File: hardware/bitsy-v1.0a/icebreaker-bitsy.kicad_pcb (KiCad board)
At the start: 4 copper layers, 35.6 x 17.8 mm, 94 parts, among them J1 3V3, J10 4, J11 1, J12 5, J13 7, J14 6, J15 16, J16 15, J17 18, J18 17, J19 19, J2 3V3, J20 20, J21 21, J22 22, J23 23, J24 8, J25 9, J26 13, J27 14, J28 12, J29 11, J3 VIN, J30 10, J31 CDONE, J32 CRESET, J33 USB_C, J34 PROG, J4 GND, J5 GND, J6 GND, J7 2, J8 3, J9 0, P1 UP, P2 UP, P3 UP, P4 UP, SW1 TACT, U1 USBLC6-2, U2 TLV75512PDRV, U3 TLV75533PDRV, U4 LY68L6400, U5 W25Q, U6 ICE40UP5K-SG48, X1 12MHz

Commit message: Final bitsy-v1.0a
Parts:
- added REF**: Symbol_CC-SA_SilkScreen_1mm, pkl_logos:Symbol_CC-SA_SilkScreen_1mm, B.Cu at (42.5, 50.6)
- added REF**: Symbol_CC-BY_SilkScreen_1mm, pkl_logos:Symbol_CC-BY_SilkScreen_1mm, B.Cu at (42.5, 49.4)
- added REF**: Symbol_CC_SilkScreen_2mm, pkl_logos:Symbol_CC_SilkScreen_2mm, B.Cu at (43.0, 47.7)
- J33: footprint Connector_USB:USB_C_Receptacle_HRO_TYPE-C-31-M-12 -> pkl_connectors:USB_C_Receptacle_HRO_TYPE-C-31-M-12
- JP1, JP5: footprint pkl_jumpers:J_NC_0603_20x2 -> pkl_jumpers:J_NC_0603_40
- moved JP1 0.64 mm to (36.5, 45.0), turned to 90 degrees
- moved JP2 0.50 mm to (44.0, 46.0)
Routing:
- net VBUS: track 16.1 -> 21.9 mm, vias 3 -> 2
- net VIN: track 23.7 -> 24.8 mm
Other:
- board text added: "BY"
- board text added: "SA"
- board text added: "by Jordi @0xdec"
- board text added: "v1.0a"
- board text removed: "CC BY-SA"
- board text removed: "USB"
- board text removed: "V1.0a"

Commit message: WIP pin shuffling
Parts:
- removed the J11 at (36.4, 55.1)
- added J10: 3, pkl_pin_headers:Pin_Header_Straight_Round_1x01_Castellated, F.Cu at (41.4, 55.1)
- J7: renamed from J8; value 3 -> 2
- J8: renamed from J7; value 2 -> 0
- J9: value 0 -> 1
- moved R1 5.91 mm to (37.1, 52.9), turned to 270 degrees
- moved J8 5.08 mm to (33.8, 55.1)
- moved J7 2.54 mm to (38.9, 55.1)
- moved J9 2.54 mm to (36.4, 55.1)
- moved C7 0.78 mm to (53.3, 52.5), turned to 90 degrees
- renumbered J10 to J11, J14 to J13, J13 to J14, J16 to J15, J15 to J16, J19 to J18, J18 to J19, J30 to J26, J29 to J27, J26 to J29, J27 to J30
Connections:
- net /IOB_3B_G6 renamed /IOB_3b_G6
- net /IOB_6A renamed /IOB_6a
- net /IOT_38B renamed /IOT_38b
- net /IOT_42B renamed /IOT_42b
- net /IOT_43A renamed /IOT_43a
- net /IOT_44B renamed /IOT_44b
- net /iCE_SS_B renamed /iCE_SS
- J11 pad 1: /IOB_4A -> /IOB_5b
- J13 pad 1: /IOB_9B -> /IOB_8a
- J14 pad 1: /IOB_8A -> /IOB_9b
- J15 pad 1: /IOT_37A -> /IOT_36b
- J16 pad 1: /IOT_36B -> /IOT_37a
- J18 pad 1: /IOT_41A -> /IOT_39a
- J19 pad 1: /IOT_39A -> /IOT_41a
- J23 pad 1: /IOT_48B -> /IOT_50b
- J24 pad 1: /IOB_13B -> /IOB_13b
- J25 pad 1: /IOB_16A -> /IOB_18a
- J26 pad 1: /IOB_31B -> /IOB_20a
- J27 pad 1: /IOB_29B -> /IOB_22a
- J28 pad 1: /IOB_25B_G3 -> /IOB_23b
- J30 pad 1: /IOB_23B -> /IOB_25b_G3
- J7 pad 1: /IOB_2A -> /IOB_0a
- J8 pad 1: /IOB_0A -> /IOB_2a
- U6 pad 10: /~UBTN -> /IOB_18a
- U6 pad 11: /~LEDR -> /IOB_20a
- U6 pad 12: /FLASH_~WP~-IO2 -> /IOB_22a
- U6 pad 13: /FLASH_~HLD~-IO3 -> /~LEDR
- U6 pad 18: /IOB_31B -> /FLASH_~WP~-IO2
- U6 pad 19: /IOB_29B -> /FLASH_~HLD~-IO3
- U6 pad 20: /IOB_25B_G3 -> /IOB_25b_G3
- U6 pad 21: /IOB_23B -> /IOB_23b
- U6 pad 23: /IOT_37A -> /IOT_37a
- U6 pad 25: /IOT_36B -> /IOT_36b
- U6 pad 26: /IOT_39A -> /IOT_39a
- U6 pad 28: /IOT_41A -> /IOT_41a
- U6 pad 3: /IOB_9B -> /IOB_9b
- U6 pad 36: /IOT_48B -> /~UBTN
- U6 pad 37: /~LEDG -> /USB_DET
- U6 pad 38: /USB_DET -> /IOT_50b
- U6 pad 4: /IOB_8A -> /IOB_8a
- U6 pad 45: /IOB_5B -> /IOB_5b
- U6 pad 46: /IOB_0A -> /IOB_0a
- U6 pad 47: /IOB_2A -> /IOB_2a
- U6 pad 48: /IOB_4A -> /IOB_4a
- U6 pad 6: /IOB_13B -> /~LEDG
- U6 pad 9: /IOB_16A -> /IOB_13b
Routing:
- net /~LEDR: track 67.9 -> 0.00 mm, vias 5 -> 0
- net /RAM_SS: track 28.2 -> 0.00 mm, vias 3 -> 0
- net /IOB_25B_G3: track 17.1 -> 0.00 mm, vias 1 -> 0
- net /IOB_23b: track 0.00 -> 16.9 mm, vias 0 -> 1
- net /IOB_29B: track 14.5 -> 0.00 mm, vias 1 -> 0
- net /IOB_25b_G3: track 0.00 -> 14.2 mm, vias 0 -> 1
- net /IOB_3b_G6: track 15.1 -> 0.99 mm
- net /IOB_31B: track 13.6 -> 0.00 mm, vias 1 -> 0
- net /IOB_23B: track 13.5 -> 0.00 mm, vias 1 -> 0
- net /~UBTN: track 20.1 -> 7.31 mm, vias 2 -> 0
- net /IOB_5B: track 12.4 -> 0.00 mm, vias 1 -> 0
- net /IOB_22a: track 0.00 -> 12.4 mm
- net /IOT_48B: track 12.1 -> 0.00 mm, vias 1 -> 0
- net /IOB_0A: track 10.6 -> 0.00 mm, vias 1 -> 0
- net /IOB_20a: track 0.00 -> 10.3 mm
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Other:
- board text added: "+"
- board text added: "+IOB_22a 12 11"
- board text added: "+IOB_2a 47 00"
- board text added: "+IOB_4a 48 03"
- board text added: "+IOB_8a 04 06"
- board text added: "-"
- board text added: "-IOB_23b 21 12"
- board text added: "-IOB_5b 45 04"
- board text added: "-IOB_9b 03 07"
- board text added: "/"
- board text added: "13 13 IOB_24a+ ~LEDR"
- board text added: "14 20 IOB_25b- G3"
- board text added: "15 25 IOT_36b-"
- board text added: "16 23 IOT_37a+"
- board text added: "17 28 IOT_41a"
- board text added: "18 27 IOT_38b-"
- board text added: "19 26 IOT_39a+"
- board text added: "20 31 IOT_42b-"
- board text added: "21 32 IOT_43a+"
- board text added: "22 34 IOT_44b"
- board text added: "23 38 IOT_50b"
- board text added: "25"
- board text added: "26"
- board text added: "27"
- board text added: "28"
- board text added: "31"
- board text added: "32"
- board text added: "34"
- board text added: "36"
- board text added: "44"
- board text added: "45"
- board text added: "46"
- board text added: "47"
- board text added: "48"
- board text added: "G6 -IOB_3b 44 01"
- board text added: "IOB_0a 46 02"
- board text added: "IOB_16a 09 08"
- board text added: "IOB_18a 10 09"
- board text added: "IOB_20a 11 10"
- board text added: "IOB_6a 02 05"
- board text added: "R"
- board text removed: "0"
- board text removed: "1"
- board text removed: "10"
- board text removed: "11"
- board text removed: "13"
- board text removed: "13 IOB_20A-~LEDR"
- board text removed: "14"
- board text removed: "14 IOB_23B"
- board text removed: "15"
- board text removed: "15 IOT_37A"
- board text removed: "16"
- board text removed: "16 IOT_36B"
- board text removed: "17"
- board text removed: "17 IOT_39A"
- board text removed: "18 IOT_38B"
- board text removed: "19 IOT_41A"
- board text removed: "20 IOT_42B"
- board text removed: "21 IOT_43A"
- board text removed: "22"
- board text removed: "22 IOT_44B"
- board text removed: "23 IOT_48B"
- board text removed: "5"
- board text removed: "7"
- board text removed: "8"
- board text removed: "IOB_0A 02"
- board text removed: "IOB_13B 08"
- board text removed: "IOB_16A 09"
- board text removed: "IOB_25B_G3 12"
- board text removed: "IOB_29B 11"
- board text removed: "IOB_2A 03"
- board text removed: "IOB_31B 10"
- board text removed: "IOB_3B_G6 00"
- board text removed: "IOB_4A 04"
- board text removed: "IOB_5B 01"
- board text removed: "IOB_6A 05"
- board text removed: "IOB_8A 07"
- board text removed: "IOB_9B 06"

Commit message: Final bitsy-v1.0a (for real this time)
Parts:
- removed C20: 10u, pkl_dipol:C_0603
- removed J34: PROG, pkl_pin_headers:PinHeader_2x05_P2.54mm_Vertical_SMD
- removed JP7, JP8: Jumper, pkl_jumpers:J_NC_0603_30
- removed R15: 2k2, pkl_dipol:R_0402
- added J0: 0, pkl_pin_headers:Pin_Header_Straight_Round_1x01_Castellated, F.Cu at (103.8, 107.6)
- added REF**: 1b2_Logo_SilkS_2mm, pkl_logos:1b2_Logo_SilkS_2mm, F.Cu at (122.4, 104.9)
- C1: value 4u7 -> 1u; footprint pkl_dipol:C_0603 -> pkl_dipol:C_0402
- C19: value 100n -> 10u; footprint pkl_dipol:C_0402 -> pkl_dipol:C_0603
- C3: value 1u -> 4u7; footprint pkl_dipol:C_0402 -> pkl_dipol:C_0603
- J1: value 3V3 -> 1
- J10: value 3 -> 10
- J11: value 4 -> 11
- J12: value 5 -> 12
- J13: value 6 -> 13
- J14: value 7 -> 14
- J17: value 18 -> 17
- J18: value 19 -> 18
- J19: value 17 -> 19
- J2: value 3V3 -> 2
- J24: value 8 -> GND
- J25: value 9 -> GND
- J26: value 10 -> GND
- J27: value 11 -> 3V3
- J28: value 12 -> 3V3
- J29: value 13 -> VIN
- J3: value VIN -> 3
- J30: value 14 -> CDONE
- J31: value CDONE -> CRESET
- J32: value CRESET -> PROG; footprint pkl_pin_headers:Pin_Header_Straight_Round_1x01_Castellated -> pkl_pin_headers:PinHeader_2x05_P2.54mm_Vertical_SMD; moved to B.Cu
- J4: value GND -> 4
- J5: value GND -> 5
- J6: value GND -> 6
- J7: value 2 -> 7
- J8: value 0 -> 8
- J9: value 1 -> 9
- JP5: footprint pkl_jumpers:J_NC_0603_40 -> pkl_jumpers:J_NC_0603_30
- R10: value 100E -> 10k
- R11, R12: value 10k -> 330E
- R13: value 330E -> 2k2
- R14: value 330E -> 100E
- R8: footprint pkl_dipol:R_Array_Convex_4x0402 -> pkl_dipol:R_0402
- R9: footprint pkl_dipol:R_0402 -> pkl_dipol:R_Array_Convex_4x0402
- U2: value TLV75512PDRV -> TLV75533PDRV
- U3: value TLV75533PDRV -> TLV75512PDRV
- moved R9 110.7 mm to (134.1, 105.0), turned to 180 degrees
- moved J6 108.9 mm to (119.0, 107.6), turned to 0 degrees
- moved J3 104.9 mm to (111.4, 107.6), turned to 0 degrees
- moved R13 104.5 mm to (125.1, 95.4), turned to 90 degrees
- moved J8 104.5 mm to (124.1, 107.6)
- moved J9 104.5 mm to (126.7, 107.6)
- moved J10 102.3 mm to (129.2, 107.6)
- moved J11 102.3 mm to (131.8, 107.6)
- moved J12 102.3 mm to (134.3, 107.6)
- moved C8 99.5 mm to (124.6, 96.8), turned to 0 degrees
- moved JP2 98.2 mm to (123.6, 103.5), turned to 90 degrees
- moved J4 98.0 mm to (114.0, 107.6)
- moved J7 98.0 mm to (121.6, 107.6)
- moved J1 97.4 mm to (106.3, 107.6), turned to 0 degrees
- moved C5 95.1 mm to (114.5, 103.9), turned to 270 degrees
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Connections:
- net /~LEDG renamed /IOB_13b-~LEDG
- C1 pad 1: VIN -> /3V3_EN
- C11 pad 1: /VCCIO_1 -> +3V3
- C13 pad 1: VCC -> +1V2
- C14 pad 1: VCC -> +1V2
- C15 pad 1: VCC -> +1V2
- C16 pad 1: VCC -> +1V2
- C17 pad 1: VCC -> +1V2
- C18 pad 1: VCC -> +1V2
- C2 pad 1: +1V2 -> VIN
- C3 pad 1: /3V3_EN -> +3V3
- C5 pad 1: +3V3 -> +1V2
- C8 pad 1: +3V3 -> /VPP_2V5
- C9 pad 1: /VPP_2V5 -> /VCCPLL
- D1 pad C: /~LEDR -> /IOT_36b-~LEDR
- D3 pad A: /iCE_CDONE -> /CDONE
- D4 pad 1: /~RGB2 -> /~RGB0
- D4 pad 2: /~RGB0 -> /~RGB2
- J1 pad 1: +3V3 -> /IOB_3b_G6
- J10 pad 1: /IOB_4a -> /IOB_23b
- J11 pad 1: /IOB_5b -> /IOB_24a
- J12 pad 1: /IOB_6a -> /IOB_25b_G3
- J13 pad 1: /IOB_8a -> /IOT_36b-~LEDR
- J14 pad 1: /IOB_9b -> /IOT_37a
- J15 pad 1: /IOT_36b -> /IOT_38b
- J16 pad 1: /IOT_37a -> /IOT_39a
- J17 pad 1: /IOT_38b -> /IOT_41a
- J18 pad 1: /IOT_39a -> /IOT_42b
- J19 pad 1: /IOT_41a -> /IOT_43a
- J2 pad 1: +3V3 -> /IOB_4a
- J20 pad 1: /IOT_42b -> /IOT_44b
- J21 pad 1: /IOT_43a -> /IOT_48b
- J22 pad 1: /IOT_44b -> /IOT_49a
- J23 pad 1: /IOT_50b -> /IOB_0a
- J24 pad 1: /IOB_13b -> GND
- J25 pad 1: /IOB_18a -> GND
- J26 pad 1: /IOB_20a -> GND
- J27 pad 1: /IOB_22a -> +3V3
- J28 pad 1: /IOB_23b -> +3V3
- J29 pad 1: /~LEDR -> VIN
- J3 pad 1: VIN -> /IOB_5b
- J30 pad 1: /IOB_25b_G3 -> /CDONE
- J31 pad 1: /iCE_CDONE -> /~CRESET
- J32 pad 1: /iCE_CRESET -> /CDONE
- J4 pad 1: GND -> /IOB_8a
- J5 pad 1: GND -> /IOB_9b
- J6 pad 1: GND -> /IOB_16a
- J7 pad 1: /IOB_0a -> /IOB_18a
- J8 pad 1: /IOB_2a -> /IOB_20a
- J9 pad 1: /IOB_3b_G6 -> /IOB_22a
- JP2 pad 1: /RAM_SS -> /RAM_~CS
- JP3 pad 1: /FLASH_SS -> /FLASH_~CS
- JP3 pad 2: /iCE_SS -> /SPI_~CS
- JP5 pad 1: VCC -> /VCCIO_0
- JP5 pad 2: +1V2 -> +3V3
- JP6 pad 1: /VCCIO_0 -> /VCCIO_2
- R10 pad 1: /VCCPLL -> /~BTN
- R10 pad 2: VCC -> /VCCIO_2
- R11 pad 1: /iCE_CRESET -> Net-(D1-PadA)
- R12 pad 1: /~UBTN -> Net-(D2-PadA)
- R13 pad 1: Net-(D1-PadA) -> /CDONE
- R14 pad 1: Net-(D2-PadA) -> /VCCPLL
- R14 pad 2: +3V3 -> +1V2
- R8 pad 2: /FLASH_~HLD~-IO3 -> /CLK_EN
- R9 pad 2: /CLK_EN -> /FLASH_~CS
- SW1 pad 1: /~UBTN -> /~BTN
- U2 pad 1: +1V2 -> +3V3
- U2 pad 4: VIN -> /3V3_EN
- U3 pad 1: +3V3 -> +1V2
- U3 pad 4: /3V3_EN -> VIN
- U4 pad 1: /RAM_SS -> /RAM_~CS
- U4 pad 2: /FLASH_MISO-IO1 -> /SPI_MISO-IO1
- U4 pad 3: /FLASH_~WP~-IO2 -> /SPI_~WP~-IO2
- U4 pad 5: /FLASH_MOSI-IO0 -> /SPI_MOSI-IO0
- U4 pad 6: /iCE_SCK -> /SPI_SCK
- U4 pad 7: /FLASH_~HLD~-IO3 -> /SPI_~HLD~-IO3
- U5 pad 1: /FLASH_SS -> /FLASH_~CS
- U5 pad 2: /FLASH_MISO-IO1 -> /SPI_MISO-IO1
- U5 pad 3: /FLASH_~WP~-IO2 -> /SPI_~WP~-IO2
- U5 pad 5: /FLASH_MOSI-IO0 -> /SPI_MOSI-IO0
- U5 pad 6: /iCE_SCK -> /SPI_SCK
- U5 pad 7: /FLASH_~HLD~-IO3 -> /SPI_~HLD~-IO3
- U6 pad 13: /~LEDR -> /IOB_24a
- U6 pad 14: /FLASH_MOSI-IO0 -> /SPI_MOSI-IO0
- U6 pad 15: /iCE_SCK -> /SPI_SCK
- U6 pad 16: /iCE_SS -> /SPI_~CS
- U6 pad 17: /FLASH_MISO-IO1 -> /SPI_MISO-IO1
- U6 pad 18: /FLASH_~WP~-IO2 -> /SPI_~WP~-IO2
- U6 pad 19: /FLASH_~HLD~-IO3 -> /SPI_~HLD~-IO3
- U6 pad 2: /IOB_6a -> /~BTN
- U6 pad 22: /VCCIO_1 -> +3V3
- U6 pad 25: /IOT_36b -> /IOT_36b-~LEDR
- U6 pad 30: VCC -> +1V2
- U6 pad 36: /~UBTN -> /IOT_48b
- U6 pad 38: /IOT_50b -> /USB_N
- U6 pad 42: /USB_N -> /USB_P
- U6 pad 43: /USB_P -> /IOT_49a
- U6 pad 5: VCC -> +1V2
- U6 pad 7: /iCE_CDONE -> /CDONE
- U6 pad 8: /iCE_CRESET -> /~CRESET
- U6 pad 9: /IOB_13b -> /IOB_16a
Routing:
- net /IOT_36b-~LEDR: track 0.00 -> 41.8 mm, vias 0 -> 2
- net /FLASH_~HLD~-IO3: track 31.6 -> 0.00 mm, vias 2 -> 0
- net /~CRESET: track 0.00 -> 30.1 mm, vias 0 -> 3
- net /iCE_CRESET: track 28.6 -> 0.00 mm, vias 2 -> 0
- net /iCE_CDONE: track 26.8 -> 0.00 mm, vias 2 -> 0
- net /FLASH_~WP~-IO2: track 24.9 -> 0.00 mm, vias 2 -> 0
- net /iCE_SCK: track 23.9 -> 0.00 mm, vias 1 -> 0
- net /CDONE: track 0.00 -> 23.4 mm, vias 0 -> 2
- net /SPI_SCK: track 0.00 -> 22.5 mm, vias 0 -> 2
- net /SPI_~WP~-IO2: track 0.00 -> 21.6 mm, vias 0 -> 2
- net /SPI_MOSI-IO0: track 0.00 -> 21.5 mm, vias 0 -> 3
- net /SPI_~HLD~-IO3: track 0.00 -> 21.1 mm, vias 0 -> 2
- net /RAM_~CS: track 0.00 -> 20.0 mm, vias 0 -> 1
- net /FLASH_MISO-IO1: track 18.8 -> 0.00 mm, vias 2 -> 0
- net /FLASH_MOSI-IO0: track 18.6 -> 0.00 mm, vias 3 -> 0
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- added copper zone on In2.Cu, net +1V2
- removed copper zone on In2.Cu, net VCC
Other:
- board text added: "+D"
- board text added: "+IOB_22a 12 09"
- board text added: "+IOB_24a 13 11"
- board text added: "+IOB_4a 48 02"
- board text added: "+IOB_8a 04 04"
- board text added: "-D"
- board text added: "-IOB_23b 21 10"
- board text added: "-IOB_5b 45 03"
- board text added: "-IOB_9b 03 05"
- board text added: "10"
- board text added: "11"
- board text added: "13"
- board text added: "13 25 IOT_36b- ~LEDR"
- board text added: "14 23 IOT_37a+"
- board text added: "15 27 IOT_38b-"
- board text added: "16 26 IOT_39a+"
- board text added: "18 31 IOT_42b-"
- board text added: "19 32 IOT_43a+"
- board text added: "20 34 IOT_44b"
- board text added: "21 36 IOT_48b-"
- board text added: "22 43 IOT_49a+"
- board text added: "23 46 IOB_0a"
- board text added: "43"
- board text added: "CS"
- board text added: "F"
- board text added: "G3 -IOB_25b 20 12"
- board text added: "IOB_16a 09 06"
- board text added: "IOB_18a 10 07"
- board text added: "IOB_20a 11 08"
- board text added: "QSPI + Prog"
- board text added: "USB"
- board text added: "VccIO0"
- board text added: "VccIO2"
- board text added: "Vpp2v5"
- board text added: "by @0xdec 2020"
- board text added: "iCEBreaker bitsy"
- board text removed: "+IOB_22a 12 11"
- board text removed: "+IOB_4a 48 03"
- board text removed: "+IOB_8a 04 06"
- board text removed: "-IOB_23b 21 12"
- board text removed: "-IOB_5b 45 04"
- board text removed: "-IOB_9b 03 07"
- board text removed: "13 13 IOB_24a+ ~LEDR"
- board text removed: "14 20 IOB_25b- G3"
- board text removed: "15 25 IOT_36b-"
- board text removed: "16 23 IOT_37a+"
- board text removed: "18"
- board text removed: "18 27 IOT_38b-"
- board text removed: "19"
- board text removed: "19 26 IOT_39a+"
- board text removed: "2"
- board text removed: "20 31 IOT_42b-"
- board text removed: "2020"
- board text removed: "21 32 IOT_43a+"
- board text removed: "22 34 IOT_44b"
- board text removed: "23 38 IOT_50b"
- board text removed: "6"
- board text removed: "D+"
- board text removed: "D-"
- board text removed: "Flsh SS"
- board text removed: "IOB_0a 46 02"
- board text removed: "IOB_16a 09 08"
- board text removed: "IOB_18a 10 09"
- board text removed: "IOB_20a 11 10"
- board text removed: "IOB_6a 02 05"
- board text removed: "RAM SS"
- board text removed: "SPI Flash Prog"
- board text removed: "SS"
- board text removed: "USB TYPE-C"
- board text removed: "Vcc"
- board text removed: "Vcc IO0"
- board text removed: "Vcc IO1"
- board text removed: "Vcc IO2"
- board text removed: "Vpp 2v5"
- board text removed: "by Jordi @0xdec"

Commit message: Obfuscate
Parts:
- LOGO1: footprint pkl_logos:1b2_Logo_SilkS_6.5mm -> pkl_logos:null_Logo_SilkS_6.5mm
- REF**: value 1b2_Logo_SilkS_2mm -> null_Logo_SilkS_2mm; footprint pkl_logos:1b2_Logo_SilkS_2mm -> pkl_logos:null_Logo_SilkS_2mm
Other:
- board text added: "NULL"
- board text added: "NULL 2020"
- board text removed: "1BitSquared"
- board text removed: "by @0xdec 2020"

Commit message: Change bitsy silkscreen labels to match Teensy
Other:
- board text added: "0"
- board text added: "1"
- board text added: "14"
- board text added: "15"
- board text added: "16"
- board text added: "17"
- board text added: "18"
- board text added: "19"
- board text added: "2"
- board text added: "22"
- board text added: "5"
- board text added: "6"
- board text added: "7"
- board text added: "8"
- board text removed: "25"
- board text removed: "26"
- board text removed: "27"
- board text removed: "28"
- board text removed: "31"
- board text removed: "32"
- board text removed: "34"
- board text removed: "36"
- board text removed: "43"
- board text removed: "44"
- board text removed: "45"
- board text removed: "46"
- board text removed: "47"
- board text removed: "48"

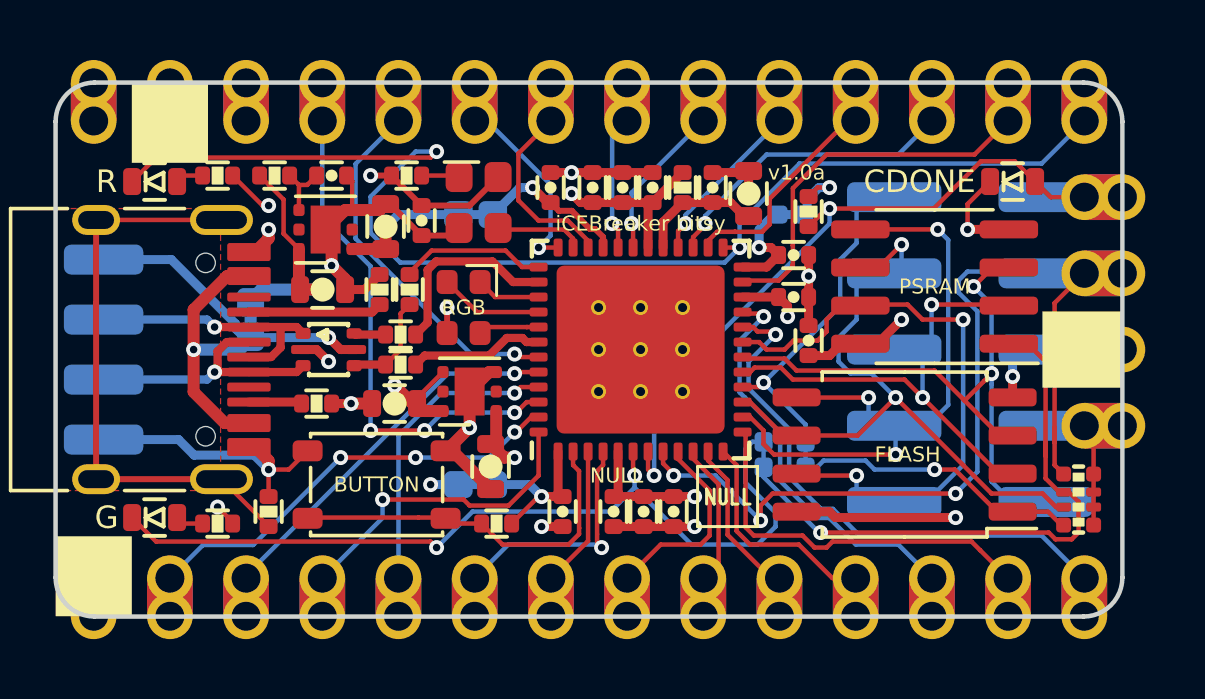
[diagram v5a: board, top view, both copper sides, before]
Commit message: Change pin labels to match Teensy
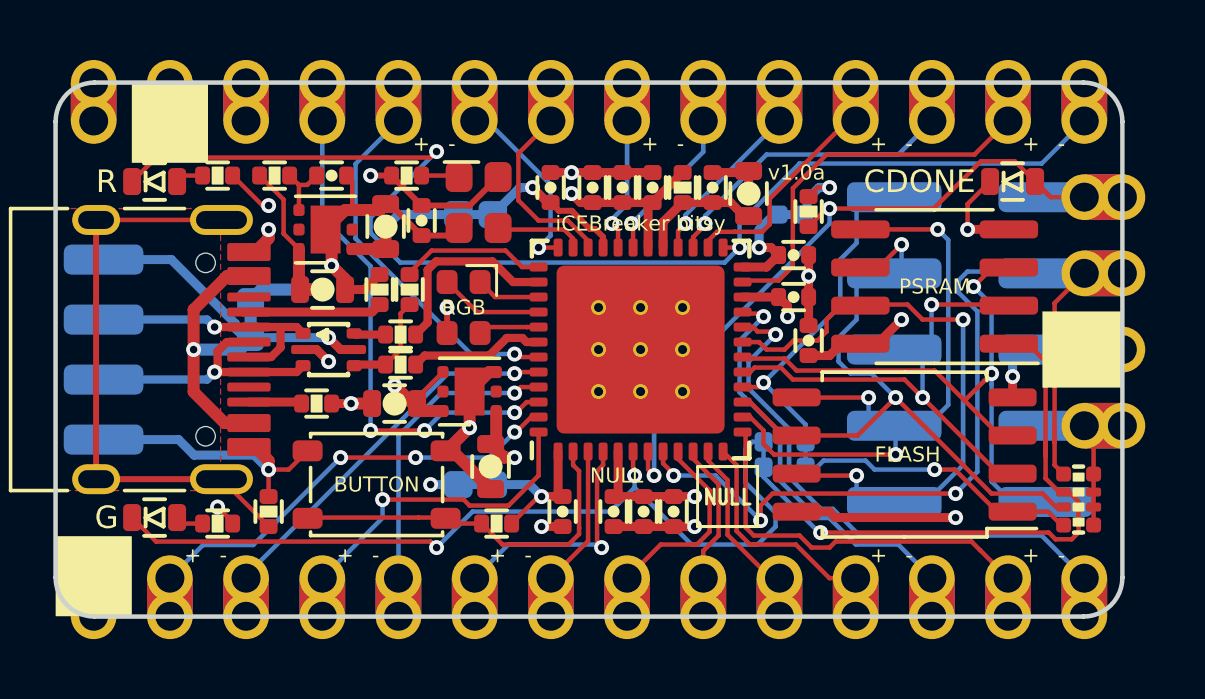
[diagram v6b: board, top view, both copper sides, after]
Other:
- board text added: "QSPI Prog"
- board text added: "by @0xdec 2020"
- board text removed: "NULL 2020"
- board text removed: "QSPI + Prog"

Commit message: Regenerate imgs and pdfs
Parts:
- LOGO1: footprint pkl_logos:null_Logo_SilkS_6.5mm -> pkl_logos:1b2_Logo_SilkS_6.5mm
- REF**: value null_Logo_SilkS_2mm -> 1b2_Logo_SilkS_2mm; footprint pkl_logos:null_Logo_SilkS_2mm -> pkl_logos:1b2_Logo_SilkS_2mm
- renumbered J33 to J1, J32 to J2, J0 to P0, J1 to P1, J10 to P10, J11 to P11, J12 to P12, J13 to P13, J14 to P14, J15 to P15, J16 to P16, J17 to P17, J18 to P18, J19 to P19, J2 to P2, J20 to P20, J21 to P21, J22 to P22, J23 to P23, J24 to P24, J25 to P25, J26 to P26, J27 to P27, J28 to P28, J29 to P29, J3 to P3, J30 to P30, J31 to P31, P1 to P32, P2 to P33, P3 to P34, P4 to P35, J4 to P4, J5 to P5, J6 to P6, J7 to P7, J8 to P8, J9 to P9
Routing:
- net /CDONE: track 23.4 -> 25.3 mm
- net /~CRESET: track 30.1 -> 29.0 mm, vias 3 -> 1
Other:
- board text added: "1BitSquared"
- board text removed: "NULL"

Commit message: Obfuscate
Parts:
- LOGO1: footprint pkl_logos:1b2_Logo_SilkS_6.5mm -> pkl_logos:null_Logo_SilkS_6.5mm
- REF**: value 1b2_Logo_SilkS_2mm -> null_Logo_SilkS_2mm; footprint pkl_logos:1b2_Logo_SilkS_2mm -> pkl_logos:null_Logo_SilkS_2mm
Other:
- board text added: "NULL"
- board text removed: "1BitSquared"
